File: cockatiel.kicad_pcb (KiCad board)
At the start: 4 copper layers, 51 x 60 mm, 39 parts, among them J1 Programmer, J10 MIC_N_BYP, J11 MIC_P_SEL, J12 MIC_N_SEL, J13 Cox Box Mic In, J14 Cox Box Mic Out, J15 Mic Out, J16 Headset/Mic In, J3 DEBUG_UART, J4 RESET, J5 Magnetic connector, J6 PWR, J7 Battery Connector, J8 LED, J9 MIC_P_BYP, T1 Transformer_Audio, U1 F-3188_CSR8645

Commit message: Correct project-specific library setup and spelling
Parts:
- T1: footprint cockateil:Transformer_Triad_T Y-141PN -> cockatiel:Transformer_Triad_T Y-141PN
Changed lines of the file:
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@@
     )
   )
-  (footprint "cockateil:Transformer_Triad_T Y-141PN" (layer "F.Cu")
+  (footprint "cockatiel:Transformer_Triad_T Y-141PN" (layer "F.Cu")
     (at 134.8621 142.974)
     (descr "NF-Transformer, 1:1, ETAL P1200,http://www.etalgroup.com/sites/default/files/products/P1200_April_2005.pdf")
@@
       (effects (font (size 1 1) (thickness 0.15)))
     )
+    (fp_line (start -2.286 -6.1595) (end 11.684 -6.1595) (layer "F.SilkS") (width 0.12))
+    (fp_line (start -2.286 -7.312356) (end -2.286 -8.943644) (layer "F.SilkS") (width 0.12))
     (fp_line (start -2.286 -5.7785) (end 11.684 -5.7785) (layer "F.SilkS") (width 0.12))
-    (fp_line (start 11.684 -4.488788) (end 11.684 -2.8575) (layer "F.SilkS") (width 0.12))
+    (fp_line (start 4.699 -6.530644) (end 4.699 -8.308644) (layer "F.SilkS") (width 0.12))
     (fp_line (start -2.286 -4.498644) (end -2.286 -2.8575) (layer "F.SilkS") (width 0.12))
-    (fp_line (start -2.286 -6.1595) (end 11.684 -6.1595) (layer "F.SilkS") (width 0.12))
-    (fp_line (start 4.699 -6.530644) (end 4.699 -8.308644) (layer "F.SilkS") (width 0.12))
     (fp_line (start 11.684 -7.3025) (end 11.684 -8.943644) (layer "F.SilkS") (width 0.12))
     (fp_line (start 4.699 -5.2705) (end 4.699 -3.4925) (layer "F.SilkS") (width 0.12))
-    (fp_line (start -2.286 -7.312356) (end -2.286 -8.943644) (layer "F.SilkS") (width 0.12))
+    (fp_line (start 11.684 -4.488788) (end 11.684 -2.8575) (layer "F.SilkS") (width 0.12))
     (fp_rect (start -5.5626 -14.478) (end 15.0622 3.302) (layer "F.SilkS") (width 0.12) (fill none))
     (fp_arc (start 0.508 -4.5085) (mid 1.905 -5.280356) (end 3.302 -4.5085) (layer "F.SilkS") (width 0.12))
     (fp_arc (start -2.286 -4.498644) (mid -0.889 -5.2705) (end 0.508 -4.498644) (layer "F.SilkS") (width 0.12))
+    (fp_arc (start 0.508 -7.312356) (mid -0.889 -6.5405) (end -2.286 -7.312356) (layer "F.SilkS") (width 0.12))
+    (fp_arc (start 6.096 -7.3025) (mid 4.699 -6.530644) (end 3.302 -7.3025) (layer "F.SilkS") (width 0.12))
     (fp_arc (start 6.096 -4.498644) (mid 7.493 -5.2705) (end 8.89 -4.498644) (layer "F.SilkS") (width 0.12))
-    (fp_arc (start 0.508 -7.312356) (mid -0.889 -6.5405) (end -2.286 -7.312356) (layer "F.SilkS") (width 0.12))
     (fp_arc (start 8.89 -7.292644) (mid 7.493 -6.520788) (end 6.096 -7.292644) (layer "F.SilkS") (width 0.12))
+    (fp_arc (start 8.89 -4.488788) (mid 10.287 -5.260644) (end 11.684 -4.488788) (layer "F.SilkS") (width 0.12))
     (fp_arc (start 3.302 -7.3025) (mid 1.905 -6.530644) (end 0.508 -7.3025) (layer "F.SilkS") (width 0.12))
-    (fp_arc (start 8.89 -4.488788) (mid 10.287 -5.260644) (end 11.684 -4.488788) (layer "F.SilkS") (width 0.12))
     (fp_arc (start 3.302 -4.498644) (mid 4.699 -5.2705) (end 6.096 -4.498644) (layer "F.SilkS") (width 0.12))
     (fp_arc (start 11.684 -7.3025) (mid 10.287 -6.530644) (end 8.89 -7.3025) (layer "F.SilkS") (width 0.12))
-    (fp_arc (start 6.096 -7.3025) (mid 4.699 -6.530644) (end 3.302 -7.3025) (layer "F.SilkS") (width 0.12))
     (fp_circle (center 1.524 -1.016) (end 1.778 -1.016) (layer "F.SilkS") (width 0.12) (fill solid))
     (fp_rect (start -5.588 -14.478) (end 14.986 3.302) (layer "F.Fab") (width 0.1) (fill none))
@@
     (pad "6" thru_hole circle (at 9.4996 -10.668) (size 1.524 1.524) (drill 0.762) (layers *.Cu *.Mask)
       (net 56 "Net-(J9-Pad1)") (pintype "passive"))
-    (group "" (id 4c94e908-ade8-4c48-9cbc-9b35a618f70e)
+    (group "" (id 9a6cc76c-ff6c-4702-8f46-45c81d7a3989)
       (members
-        14c825f1-0be3-4534-a823-734778228096
-        1d0080f9-8cf5-4ebd-9b4c-5f6891eb57f6
-        1d737dab-1750-45c2-af34-d04bb80bbc7f
-        1fa45049-3305-452e-aa2f-e578fe051e75
-        2d1d93c5-9ca9-4c00-bd8b-c5c79e0560c2
-        2dadded2-803e-49a8-b12c-c1b90c8c400d
-        45fe0cd7-408d-48d5-a872-cf105c113464
-        47eaa433-b458-4ac0-9c06-2a546db505db
-        5a1e5f75-e480-4183-9779-6a14fb9ab9e4
-        5da0d118-fd5e-4a70-95bf-db2ce817d3dd
-        6852b1d4-2402-477d-a17e-290e89148026
-        8801582a-12f3-45ce-8184-2ded8ca44e35
-        8e519f3c-2097-468f-b51e-8dd561d10d50
-        9fc4837f-f2fc-49a5-9c3b-8f0d0702d155
-        bdb56112-c9aa-4edb-a25f-761f898e8f46
-        bf077244-4e13-4bd6-a593-3c3015cab9e5
-        c9216f6f-91a1-492a-956d-325f17e4b977
-        ea5e6168-e1a6-46e8-a994-fec78bf5ef50
-        fda8ffda-eabb-477b-ba6d-329cc71f1680
+        1a4fe336-65d3-4b1c-b5a0-506874c24553
+        1c8e574e-bccf-4a25-806f-f9ba6eb39fed
+        2ed95ad1-5602-45e1-9eaf-ea5f8d432082
+        39d6d09d-ae6c-4614-bdcc-c49566d60a30
+        40304077-386c-434b-bc4f-2cdc563731fc
+        4e69e3e9-fe12-4b79-96a4-c25f44eb8336
+        528de1ca-3ef5-4665-b36e-83fb04c1b10c
+        5a9218c3-f300-41fb-874e-8f96239942a5
+        64d41639-af16-4d4c-8b09-faa403a1f654
+        9e3d7488-b0c4-483a-8cb3-88643a159675
+        a5f8fe4d-9e98-4b13-808f-68691c37e070
+        b3f7d195-ac24-44fc-a9ff-2bf80af1969d
+        b42b2a62-9766-47f1-868c-fa80f525de2b
+        c406ae52-50d1-4840-bd2b-45f4894f78ea
+        c6965724-a35f-42b9-a525-110ae2b1f950
+        d7ebc631-de7a-40ee-acfe-1a21fa8b2c31
+        dd5c83e9-fb07-439e-b477-0e164ec6f5f5
+        e5fc37c4-ba85-42c1-ae56-db4512390232
+        f84d6af4-6186-471c-80eb-11fbcb73b40d
       )
     )

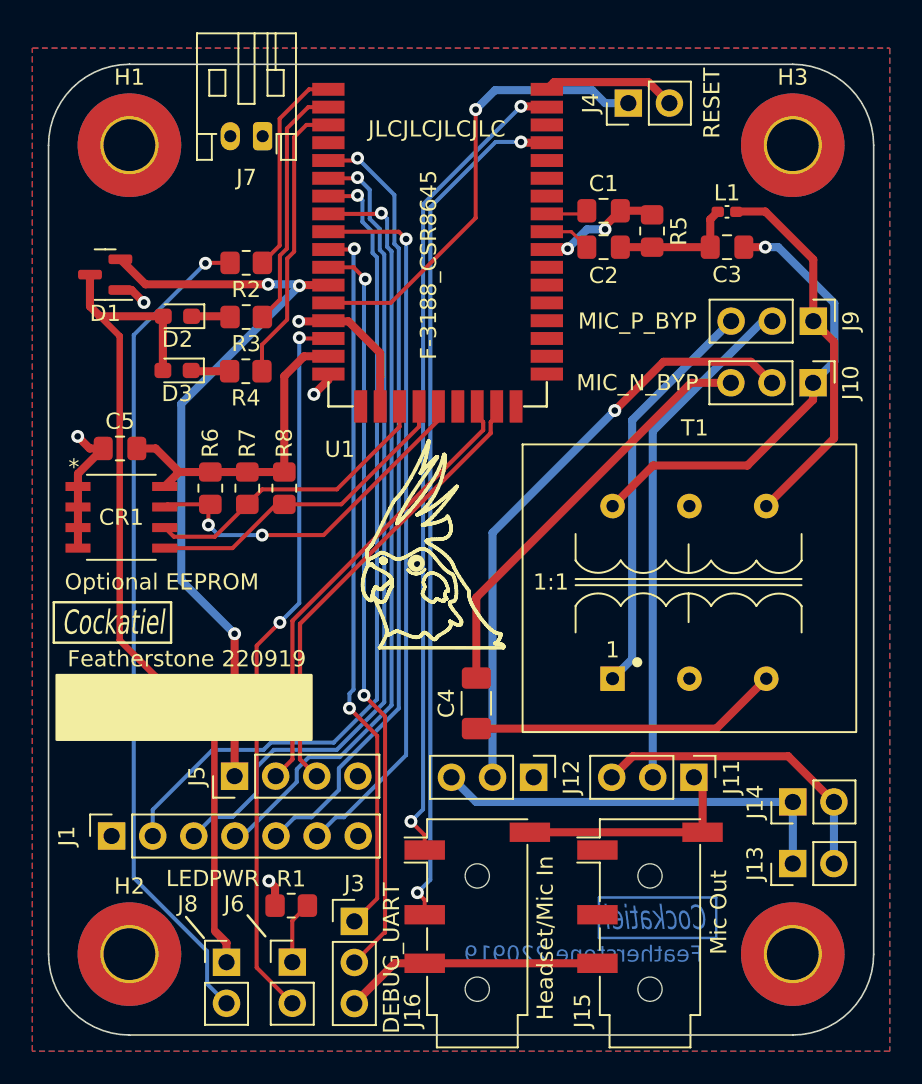
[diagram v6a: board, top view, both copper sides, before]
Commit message: WIP: reduce the board complexity and size
This in turn reduces the eBoM and board size, aiming to reduce cost of
manufacture.
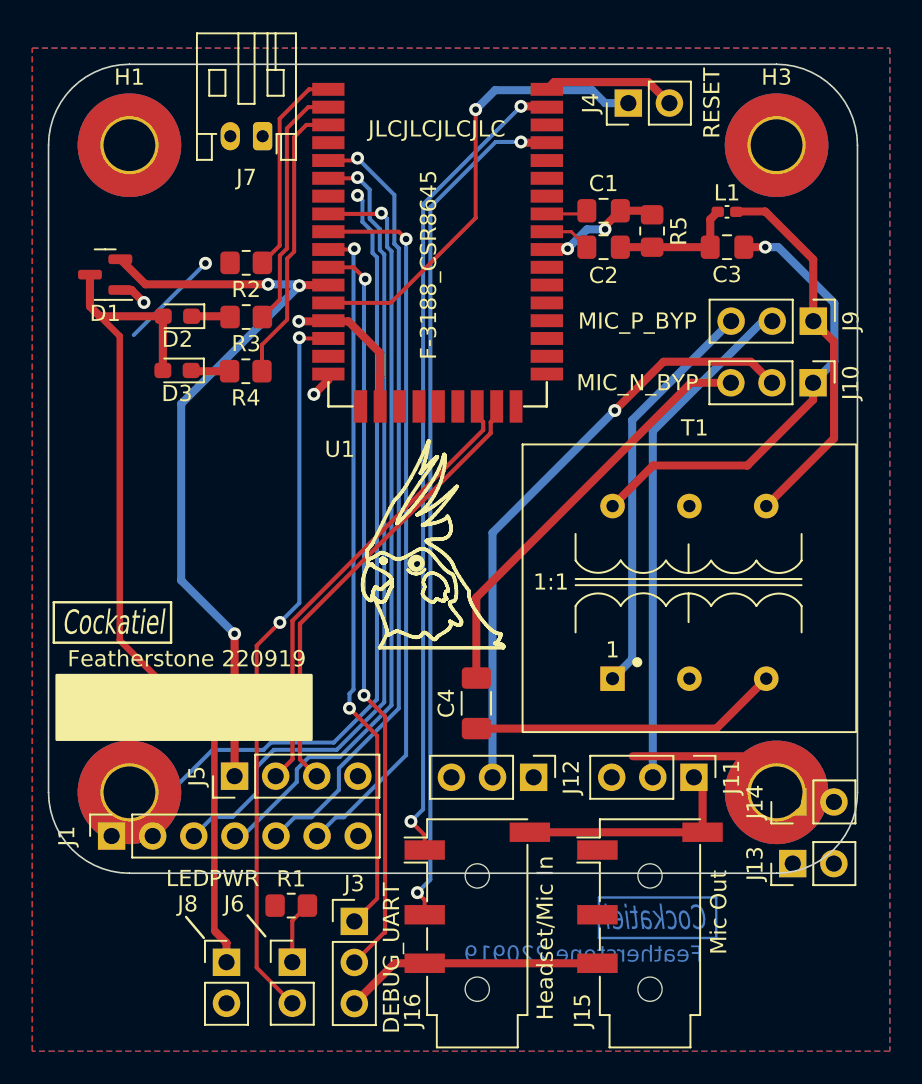
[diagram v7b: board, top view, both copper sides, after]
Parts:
- removed C5: 100n, Capacitor_SMD:C_0805_2012Metric_Pad1.18x1.45mm_HandSolder
- removed CR1: Optional EEPROM, st:M24512-RMN6P
- removed R6, R7, R8: 2K2, Resistor_SMD:R_0805_2012Metric_Pad1.20x1.40mm_HandSolder
- moved H4 10.0 mm to (145.0, 150.0)
- moved H2 10.0 mm to (105.0, 150.0)
- moved H3 1.00 mm to (145.0, 110.0)
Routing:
- net Earth: track 34.7 -> 90.2 mm, vias 2 -> 3
- net /SPI_CLK: track 51.8 -> 0.00 mm, vias 1 -> 0
- net Net-(J8-Pad2): track 51.5 -> 0.00 mm, vias 1 -> 0
- net Net-(J12-Pad3): track 25.5 -> 0.00 mm
- net /PIO12: track 22.5 -> 0.00 mm, vias 2 -> 0
- net +1V8: track 20.1 -> 0.00 mm
- net /PIO11: track 20.1 -> 0.00 mm
- net Net-(J11-Pad3): track 19.3 -> 0.00 mm
- net /PIO10: track 18.8 -> 0.00 mm
- net +BATT: track 12.6 -> 10.9 mm, vias 3 -> 2
- net Net-(J11-Pad1): track 14.3 -> 13.5 mm
- net USB_P: track 28.3 -> 27.7 mm
- net USB_N: track 28.3 -> 27.7 mm
- net Net-(J11-Pad2): track 31.6 -> 31.0 mm
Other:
- board size 51 x 60 mm -> 50 x 50 mm

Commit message: Swap the battery connector pins
It seems that the de-facto setup is with pin 1 as ground, so fix it
here.
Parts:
- removed J10: MIC_N_BYP, Connector_PinHeader_2.54mm:PinHeader_1x03_P2.54mm_Vertical
- removed J9: MIC_P_BYP, Connector_PinHeader_2.54mm:PinHeader_1x03_P2.54mm_Vertical
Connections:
- J12 pad 2: Net-(J10-Pad2) -> Net-(C4-Pad2)
- J7 pad 1: +BATT -> Earth
- J7 pad 2: Earth -> +BATT
- T1 pad 1: Net-(J9-Pad3) -> Net-(J11-Pad2)
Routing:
- net Net-(J10-Pad2): track 37.3 -> 0.00 mm, vias 1 -> 0
- net Net-(C4-Pad2): track 26.2 -> 63.5 mm, vias 0 -> 1
- net Net-(J9-Pad3): track 25.1 -> 0.00 mm
- net Net-(J11-Pad2): track 31.0 -> 56.1 mm
